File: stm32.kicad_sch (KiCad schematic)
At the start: 26 parts, among them J1 TC2030-IDC, J7 Conn_01x03, U2 STM32F410CBU6, Y3 8MHz

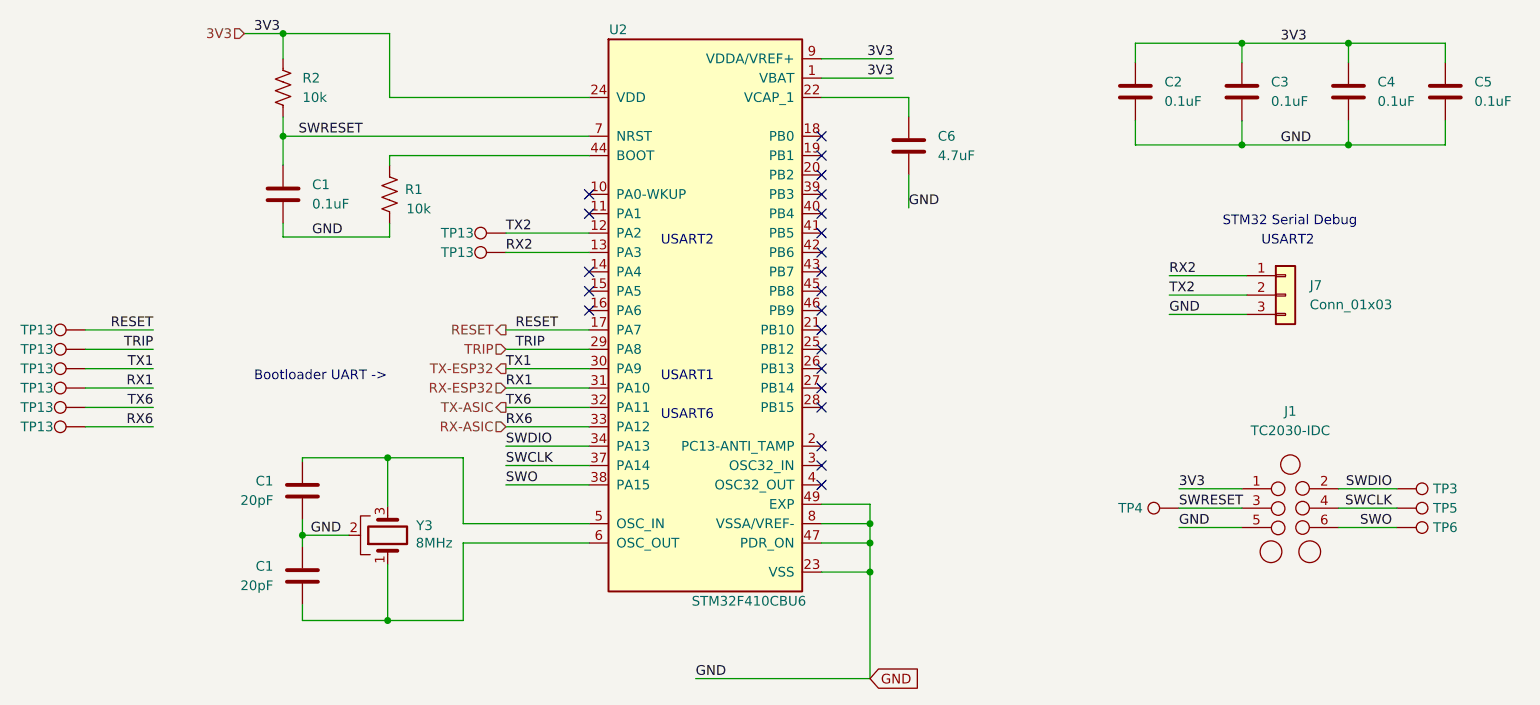
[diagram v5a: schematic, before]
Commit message: update to KiCad8, DNP 32kHz crystal
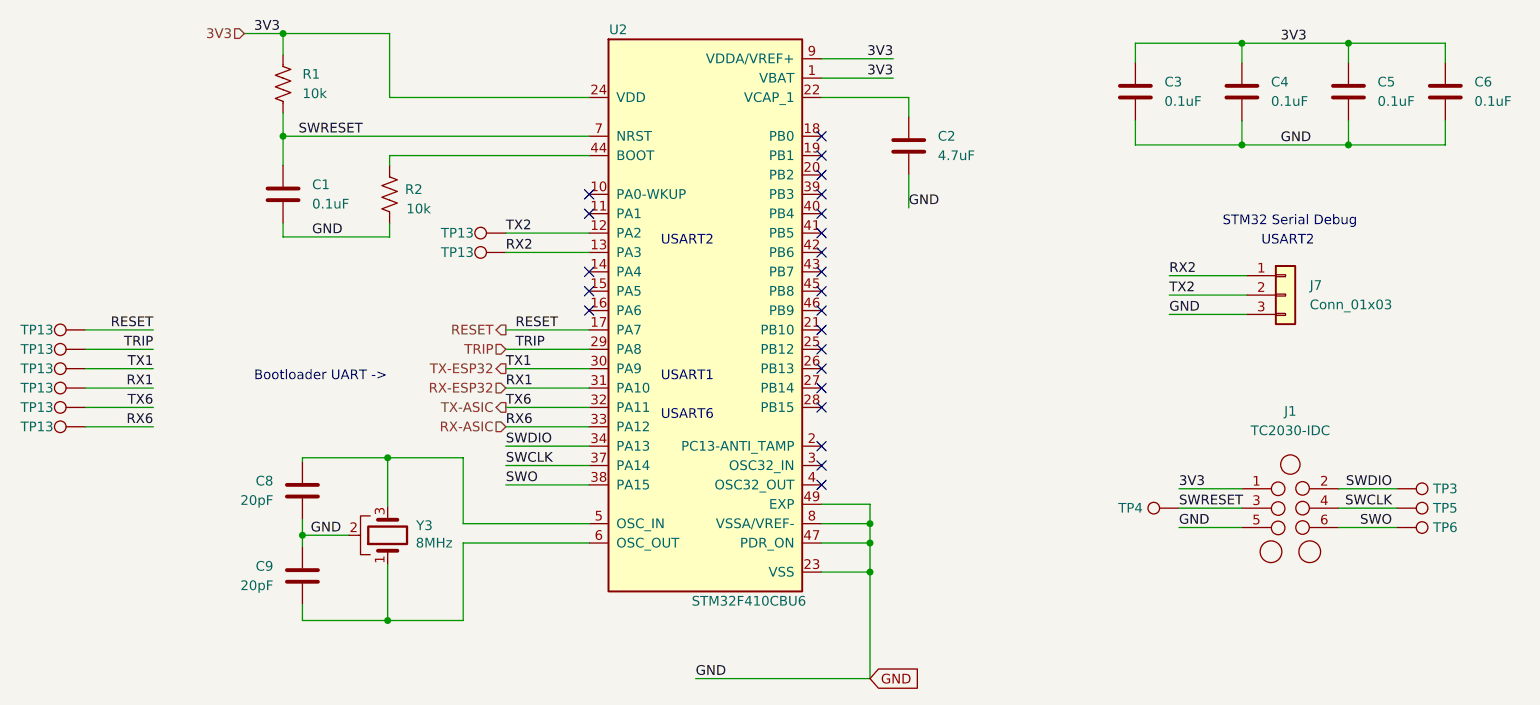
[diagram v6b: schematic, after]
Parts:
- renumbered C6 to C2, C2 to C3, C3 to C4, C4 to C5, C5 to C6, C1 to C8, C1 to C9, R2 to R1, R1 to R2
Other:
- moved on the sheet: R1
